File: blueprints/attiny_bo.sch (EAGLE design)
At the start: 8 parts, among them IC1 ATTiny85, J1 AVR_SPI_PRG_6NS

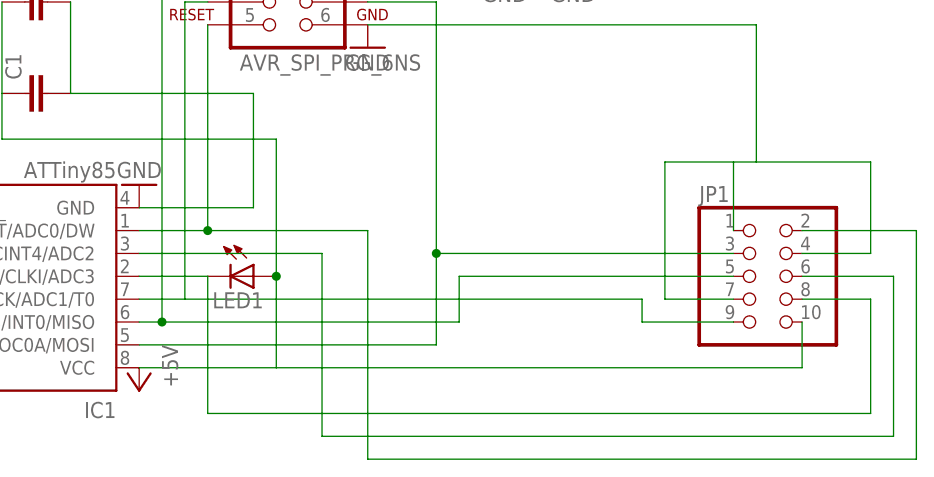
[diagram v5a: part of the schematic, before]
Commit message: rethought the signals to 5x2 header, tuned the mounting pad positions
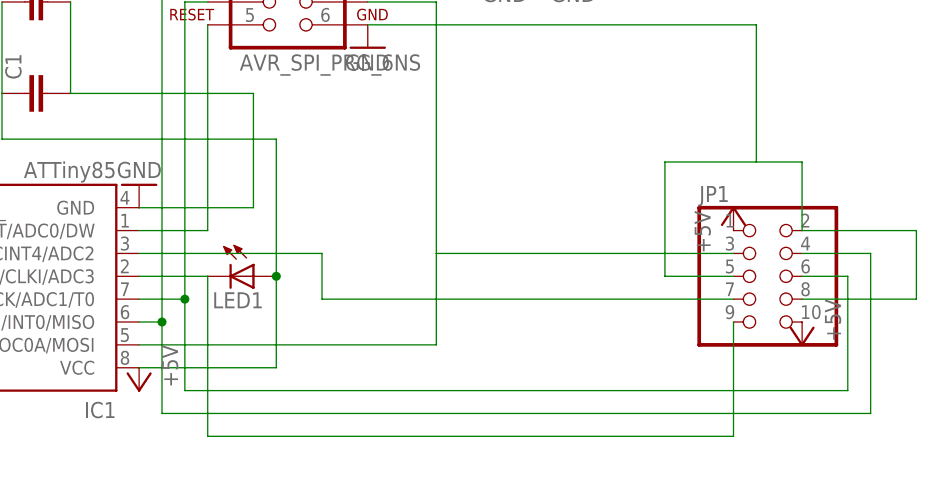
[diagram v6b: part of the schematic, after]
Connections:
- net +5V: now also JP1.1
- net GND: now also JP1.2, JP1.5, JP1.8; no longer JP1.1, JP1.4, JP1.7
- net PB1: now also JP1.4; no longer JP1.5
- net PB2: now also JP1.6; no longer JP1.9
- net PB3: now also JP1.9; no longer JP1.8
- net PB4: now also JP1.7; no longer JP1.6
- net PB5: no longer JP1.2
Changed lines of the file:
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@@
 <part name="GND1" library="supply1" deviceset="GND" device=""/>
 <part name="GND2" library="supply1" deviceset="GND" device=""/>
+<part name="P+1" library="supply1" deviceset="+5V" device=""/>
+<part name="P+2" library="supply1" deviceset="+5V" device=""/>
 </parts>
 <sheets>
@@
 <instance part="GND1" gate="1" x="99.06" y="109.22"/>
 <instance part="GND2" gate="1" x="91.44" y="109.22"/>
+<instance part="P+1" gate="1" x="116.84" y="83.82"/>
+<instance part="P+2" gate="1" x="124.46" y="68.58" rot="R180"/>
 </instances>
 <busses>
@@
 <wire x1="58.42" y1="109.22" x2="53.34" y2="109.22" width="0.1524" layer="91"/>
 <wire x1="53.34" y1="109.22" x2="53.34" y2="71.12" width="0.1524" layer="91"/>
-<wire x1="53.34" y1="71.12" x2="86.36" y2="71.12" width="0.1524" layer="91"/>
-<wire x1="86.36" y1="71.12" x2="86.36" y2="76.2" width="0.1524" layer="91"/>
+<pinref part="JP1" gate="A" pin="4"/>
+<wire x1="124.46" y1="78.74" x2="132.08" y2="78.74" width="0.1524" layer="91"/>
+<wire x1="132.08" y1="78.74" x2="132.08" y2="60.96" width="0.1524" layer="91"/>
+<wire x1="132.08" y1="60.96" x2="53.34" y2="60.96" width="0.1524" layer="91"/>
+<wire x1="53.34" y1="60.96" x2="53.34" y2="71.12" width="0.1524" layer="91"/>
 <junction x="53.34" y="71.12"/>
-<pinref part="JP1" gate="A" pin="5"/>
-<wire x1="86.36" y1="76.2" x2="116.84" y2="76.2" width="0.1524" layer="91"/>
 </segment>
 </net>
@@
 <pinref part="J1" gate="G$1" pin="6"/>
 <pinref part="GND5" gate="1" pin="GND"/>
-<pinref part="JP1" gate="A" pin="1"/>
-<wire x1="116.84" y1="81.28" x2="116.84" y2="88.9" width="0.1524" layer="91"/>
-<wire x1="119.38" y1="88.9" x2="116.84" y2="88.9" width="0.1524" layer="91"/>
 <wire x1="76.2" y1="104.14" x2="119.38" y2="104.14" width="0.1524" layer="91"/>
 <wire x1="119.38" y1="104.14" x2="119.38" y2="88.9" width="0.1524" layer="91"/>
-<wire x1="116.84" y1="88.9" x2="109.22" y2="88.9" width="0.1524" layer="91"/>
-<wire x1="109.22" y1="88.9" x2="109.22" y2="73.66" width="0.1524" layer="91"/>
-<pinref part="JP1" gate="A" pin="4"/>
-<wire x1="124.46" y1="78.74" x2="132.08" y2="78.74" width="0.1524" layer="91"/>
-<wire x1="132.08" y1="78.74" x2="132.08" y2="88.9" width="0.1524" layer="91"/>
-<wire x1="132.08" y1="88.9" x2="119.38" y2="88.9" width="0.1524" layer="91"/>
-<pinref part="JP1" gate="A" pin="7"/>
-<wire x1="116.84" y1="73.66" x2="109.22" y2="73.66" width="0.1524" layer="91"/>
+<pinref part="JP1" gate="A" pin="2"/>
+<wire x1="124.46" y1="81.28" x2="124.46" y2="88.9" width="0.1524" layer="91"/>
+<wire x1="124.46" y1="88.9" x2="119.38" y2="88.9" width="0.1524" layer="91"/>
+<wire x1="119.38" y1="88.9" x2="109.22" y2="88.9" width="0.1524" layer="91"/>
+<wire x1="109.22" y1="88.9" x2="109.22" y2="76.2" width="0.1524" layer="91"/>
+<pinref part="JP1" gate="A" pin="5"/>
+<wire x1="109.22" y1="76.2" x2="116.84" y2="76.2" width="0.1524" layer="91"/>
+<wire x1="124.46" y1="81.28" x2="137.16" y2="81.28" width="0.1524" layer="91"/>
+<wire x1="137.16" y1="81.28" x2="137.16" y2="73.66" width="0.1524" layer="91"/>
+<pinref part="JP1" gate="A" pin="8"/>
+<wire x1="137.16" y1="73.66" x2="124.46" y2="73.66" width="0.1524" layer="91"/>
 </segment>
 <segment>
@@
 <pinref part="LED1" gate="G$1" pin="A"/>
 <junction x="66.04" y="76.2"/>
-<pinref part="JP1" gate="A" pin="10"/>
-<wire x1="124.46" y1="66.04" x2="124.46" y2="71.12" width="0.1524" layer="91"/>
-<wire x1="66.04" y1="66.04" x2="124.46" y2="66.04" width="0.1524" layer="91"/>
 <pinref part="C2" gate="G$1" pin="1"/>
 <wire x1="35.56" y1="96.52" x2="35.56" y2="106.68" width="0.1524" layer="91"/>
@@
 <pinref part="J1" gate="G$1" pin="2"/>
 <pinref part="P+5" gate="1" pin="+5V"/>
+</segment>
+<segment>
+<pinref part="JP1" gate="A" pin="1"/>
+<pinref part="P+1" gate="1" pin="+5V"/>
+</segment>
+<segment>
+<pinref part="JP1" gate="A" pin="10"/>
+<pinref part="P+2" gate="1" pin="+5V"/>
 </segment>
 </net>
@@
 <pinref part="JP1" gate="A" pin="3"/>
 <wire x1="116.84" y1="78.74" x2="83.82" y2="78.74" width="0.1524" layer="91"/>
-<junction x="83.82" y="78.74"/>
 </segment>
 </net>
@@
 <wire x1="50.8" y1="81.28" x2="58.42" y2="81.28" width="0.1524" layer="91"/>
 <wire x1="58.42" y1="81.28" x2="58.42" y2="104.14" width="0.1524" layer="91"/>
-<wire x1="58.42" y1="81.28" x2="76.2" y2="81.28" width="0.1524" layer="91"/>
-<wire x1="76.2" y1="81.28" x2="76.2" y2="55.88" width="0.1524" layer="91"/>
-<wire x1="76.2" y1="55.88" x2="137.16" y2="55.88" width="0.1524" layer="91"/>
-<wire x1="137.16" y1="55.88" x2="137.16" y2="81.28" width="0.1524" layer="91"/>
-<junction x="58.42" y="81.28"/>
-<pinref part="JP1" gate="A" pin="2"/>
-<wire x1="124.46" y1="81.28" x2="137.16" y2="81.28" width="0.1524" layer="91"/>
 </segment>
 </net>
@@
 <pinref part="J1" gate="G$1" pin="3"/>
 <wire x1="55.88" y1="106.68" x2="58.42" y2="106.68" width="0.1524" layer="91"/>
-<wire x1="55.88" y1="73.66" x2="106.68" y2="73.66" width="0.1524" layer="91"/>
-<wire x1="106.68" y1="73.66" x2="106.68" y2="71.12" width="0.1524" layer="91"/>
-<pinref part="JP1" gate="A" pin="9"/>
-<wire x1="106.68" y1="71.12" x2="116.84" y2="71.12" width="0.1524" layer="91"/>
+<pinref part="JP1" gate="A" pin="6"/>
+<wire x1="124.46" y1="76.2" x2="129.54" y2="76.2" width="0.1524" layer="91"/>
+<wire x1="129.54" y1="76.2" x2="129.54" y2="63.5" width="0.1524" layer="91"/>
+<wire x1="129.54" y1="63.5" x2="55.88" y2="63.5" width="0.1524" layer="91"/>
+<wire x1="55.88" y1="63.5" x2="55.88" y2="73.66" width="0.1524" layer="91"/>
+<junction x="55.88" y="73.66"/>
 </segment>
 </net>
@@
 <pinref part="IC1" gate="G$1" pin="PB3/PCINT3/CLKI/ADC3"/>
 <wire x1="58.42" y1="76.2" x2="50.8" y2="76.2" width="0.1524" layer="91"/>
-<wire x1="58.42" y1="76.2" x2="58.42" y2="60.96" width="0.1524" layer="91"/>
-<wire x1="58.42" y1="60.96" x2="132.08" y2="60.96" width="0.1524" layer="91"/>
-<wire x1="132.08" y1="60.96" x2="132.08" y2="73.66" width="0.1524" layer="91"/>
-<pinref part="JP1" gate="A" pin="8"/>
-<wire x1="132.08" y1="73.66" x2="124.46" y2="73.66" width="0.1524" layer="91"/>
+<wire x1="58.42" y1="76.2" x2="58.42" y2="58.42" width="0.1524" layer="91"/>
+<pinref part="JP1" gate="A" pin="9"/>
+<wire x1="58.42" y1="58.42" x2="116.84" y2="58.42" width="0.1524" layer="91"/>
+<wire x1="116.84" y1="58.42" x2="116.84" y2="71.12" width="0.1524" layer="91"/>
 </segment>
 </net>
@@
 <pinref part="IC1" gate="G$1" pin="PB4/PCINT4/ADC2"/>
 <wire x1="50.8" y1="78.74" x2="71.12" y2="78.74" width="0.1524" layer="91"/>
-<wire x1="71.12" y1="78.74" x2="71.12" y2="58.42" width="0.1524" layer="91"/>
-<wire x1="71.12" y1="58.42" x2="134.62" y2="58.42" width="0.1524" layer="91"/>
-<wire x1="134.62" y1="58.42" x2="134.62" y2="76.2" width="0.1524" layer="91"/>
-<pinref part="JP1" gate="A" pin="6"/>
-<wire x1="124.46" y1="76.2" x2="134.62" y2="76.2" width="0.1524" layer="91"/>
+<wire x1="71.12" y1="78.74" x2="71.12" y2="73.66" width="0.1524" layer="91"/>
+<pinref part="JP1" gate="A" pin="7"/>
+<wire x1="71.12" y1="73.66" x2="116.84" y2="73.66" width="0.1524" layer="91"/>
 </segment>
 </net>
